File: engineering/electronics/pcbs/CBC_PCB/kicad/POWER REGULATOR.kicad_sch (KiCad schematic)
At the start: 69 parts, among them U23 MP9486GN-Z, U27 10mΩ, U29 1uF, U30 1uH, U9 120pF

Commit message: fix: restore CBC schematic library nicknames
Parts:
- C15: symbol CBC_PCB:CC0805KRX7R0BB471 -> EasyEDA_Lib:CC0805KRX7R0BB471
- C35, C41, C43, C44, C45: symbol CBC_PCB:CL10B104KC8NNNC -> EasyEDA_Lib:CL10B104KC8NNNC
- C37, C39, C62, C75, C76: symbol CBC_PCB:ERJ1KM2R2D11OT -> EasyEDA_Lib:ERJ1KM2R2D11OT
- C38, C40, C74: symbol CBC_PCB:CL21A475KBQNNNE -> EasyEDA_Lib:CL21A475KBQNNNE
- C42, C46: symbol CBC_PCB:TAJB106K025RNJ -> EasyEDA_Lib:TAJB106K025RNJ
- C59, C60, C61, C7, C73: symbol CBC_PCB:GRM31CC72A475KE11L -> EasyEDA_Lib:GRM31CC72A475KE11L
- C63: symbol CBC_PCB:CL10B224KB8NNNC -> EasyEDA_Lib:CL10B224KB8NNNC
- C64, C66, C69, C70, C71, C72, C77: symbol CBC_PCB:GRM31CR61E476ME44L -> EasyEDA_Lib:GRM31CR61E476ME44L
- C65: symbol CBC_PCB:CL10B333KB8NNNC -> EasyEDA_Lib:CL10B333KB8NNNC
- C67: symbol CBC_PCB:CL10C470JB8NNNC -> EasyEDA_Lib:CL10C470JB8NNNC
- C68: symbol CBC_PCB:AC0603KRX7R0BB472 -> EasyEDA_Lib:AC0603KRX7R0BB472
- D14: symbol CBC_PCB:FSV10150V -> EasyEDA_Lib:FSV10150V
- D15: symbol CBC_PCB:SMBJ5.0CA_C83323 -> EasyEDA_Lib:SMBJ5.0CA_C83323
- D16, D19: symbol CBC_PCB:BAV20W-7-F -> EasyEDA_Lib:BAV20W-7-F
- D17: symbol CBC_PCB:SMBJ85A-13-F -> EasyEDA_Lib:SMBJ85A-13-F
- D18: symbol CBC_PCB:CMMR1U-02 TR PBFREE -> EasyEDA_Lib:CMMR1U-02 TR PBFREE
- D20: symbol CBC_PCB:SMB5350B -> EasyEDA_Lib:SMB5350B
- D21: symbol CBC_PCB:SMBJ5365B-TP -> EasyEDA_Lib:SMBJ5365B-TP
- L4: symbol CBC_PCB:ZEMS0850-330M -> EasyEDA_Lib:ZEMS0850-330M
- L5: symbol CBC_PCB:PA1736NL -> EasyEDA_Lib:PA1736NL
- L6: symbol CBC_PCB:PSPMAA1082T-220M-CGP -> EasyEDA_Lib:PSPMAA1082T-220M-CGP
- Q8, Q9: symbol CBC_PCB:SP015N03BGHTO -> EasyEDA_Lib:SP015N03BGHTO
- R30, R33: symbol CBC_PCB:RT0603BRD0710KL -> EasyEDA_Lib:RT0603BRD0710KL
- R31: symbol CBC_PCB:RT0603BRE07240KL -> EasyEDA_Lib:RT0603BRE07240KL
- R32: symbol CBC_PCB:PTFR0603B140KP9 -> EasyEDA_Lib:PTFR0603B140KP9
- R36: symbol CBC_PCB:RC0402FR-070RL -> EasyEDA_Lib:RC0402FR-070RL
- R37: symbol CBC_PCB:FRC0805F1204TS -> EasyEDA_Lib:FRC0805F1204TS
- R38: symbol CBC_PCB:PTFR0603B51K0P9 -> EasyEDA_Lib:PTFR0603B51K0P9
- R39: symbol CBC_PCB:0805W8F1603T5E -> EasyEDA_Lib:0805W8F1603T5E
- R40: symbol CBC_PCB:0603WAF6041T5E -> EasyEDA_Lib:0603WAF6041T5E
- R41, R45: symbol CBC_PCB:0805W8F300KT5E -> EasyEDA_Lib:0805W8F300KT5E
- R42: symbol CBC_PCB:FRC0603F7501TS -> EasyEDA_Lib:FRC0603F7501TS
- R43: symbol CBC_PCB:0603WAF6042T5E -> EasyEDA_Lib:0603WAF6042T5E
- R44: symbol CBC_PCB:FRC0603F2371TS -> EasyEDA_Lib:FRC0603F2371TS
- R5: symbol CBC_PCB:PTFR0603B100RN9 -> EasyEDA_Lib:PTFR0603B100RN9
- R6: symbol CBC_PCB:ERA6AEB680V -> EasyEDA_Lib:ERA6AEB680V
- U23: symbol CBC_PCB:MP9486GN-Z -> MP9486GN-Z:MP9486GN-Z
- U24: symbol CBC_PCB:AMS1117-3.3 -> EasyEDA_Lib:AMS1117-3.3
- U27: symbol CBC_PCB:YLRY06-1-10F -> EasyEDA_Lib:YLRY06-1-10F
- U28: symbol CBC_PCB:LT8309ES5#TRMPBF -> EasyEDA_Lib:LT8309ES5#TRMPBF
- U29: symbol CBC_PCB:CC0805KKX7R0BB105 -> EasyEDA_Lib:CC0805KKX7R0BB105
- U30: symbol CBC_PCB:XAL6030-102MEC -> EasyEDA_Lib:XAL6030-102MEC
- U8: symbol CBC_PCB:LT3748EMS#PBF -> EasyEDA_Lib:LT3748EMS#PBF
- U9: symbol CBC_PCB:GCM1885C2A121FA16D -> EasyEDA_Lib:GCM1885C2A121FA16D
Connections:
- net +3V3: now also C45.1, C46.1, U24.2 (VOUT), U24.4 (VOUT)
- net +5V: now also C35.2, C38.2, C40.2, C42.1, C44.1, C74.2, L4.2, R31.2, U24.3 (VIN)
- net 12V_ISOLATED: now also C71.2, C72.2, C75.1, C76.1, C77.2, D20.1, U30.2
- net GND: now also C15.1, C37.2, C38.1, C39.2, C40.1, C42.2, C43.1, C44.2, C45.2, C46.2, C59.1, C60.1, C61.1, C62.2, C63.1, C64.1, C65.1, C67.1, C68.1, C7.1, C74.1, D14.1 (A), D14.2 (A), D15.1 (K), L5.6, R30.1, R33.1, R38.1, R40.1, R43.1, U23.8 (GND), U24.1 (GND), U27.1, U8.8 (GND), U8.9 (GND)
- net GNDE: now also C66.1, C68.2, C69.1, C70.1, C71.1, C72.1, C73.1, C75.2, C76.2, C77.1, D20.2, D21.2 (A), Q9.2 (S), Q9.3 (S), Q9.4 (S), Q9.5 (S), Q9.6 (S), Q9.7 (S), Q9.8 (S), U28.2 (GND), U29.1
- net H_PWR-IN: now also C37.1, C39.1, C64.2, L6.1, R32.2, U23.3 (VIN)
- net INTVCC: now also C61.2, R6.1, U8.5 (INTVCC)
- new net: C73.2, U28.3 (INTVCC)
- new net: C59.2, C60.2, C62.1, C7.2, D17.2 (A), L5.3, L5.4, L6.2, R37.2, R5.2, U8.1 (VIN)
- new net: Q8.1 (G), R36.2
- new net: Q8.2 (S), Q8.3 (S), Q8.4 (S), Q8.5 (S), Q8.6 (S), Q8.7 (S), Q8.8 (S), R41.2, U27.2
- new net: D18.2 (A), L5.1, L5.2, Q8.9 (D), R39.2, U9.1
- new net: C41.1, D14.3 (K), L4.1, U23.5 (SW)
- new net: R43.2, U8.12 (TC)
- new net: C15.2, R42.2, U8.11 (VC)
- new net: C66.2, C69.2, C70.2, L5.10, L5.11, L5.12, U30.1
- new net: R5.1, U9.2
- new net: C35.1, R30.2, R31.1, U23.1 (FB)
- new net: D17.1 (K), D18.1 (K)
- new net: D19.2 (A), L5.7, L5.8, L5.9, Q9.9 (D), R44.1
- new net: R44.2, U28.5 (DRAIN)
- new net: C67.2, R41.1, U8.7 (SENSE)
- new net: C65.2, R42.1
- new net: D16.1 (C), R6.2
- new net: Q9.1 (G), U28.1 (GATE)
- new net: D21.1 (K), R45.2, U28.4 (VCC), U29.2
- new net: C63.2, U8.10 (SS)
- new net: C43.2, D15.2 (A), R32.1, R33.2, U23.6 (DIM), U23.7 (EN)
- new net: R39.1, U8.16 (RFB)
- new net: D16.2 (A), L5.5
- new net: R40.2, U8.14 (RREF)
- new net: R37.1, R38.2, U8.3 (EN/UVLO)
- new net: C41.2, U23.4 (BST)
- new net: R36.1, U8.6 (GATE)
- new net: D19.1 (C), R45.1

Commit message: fix: qualify CBC connector footprint refs
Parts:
- U23: footprint SOIC-8EP_MP9486_MNP -> CBC_PCB:SOIC-8EP_MP9486_MNP

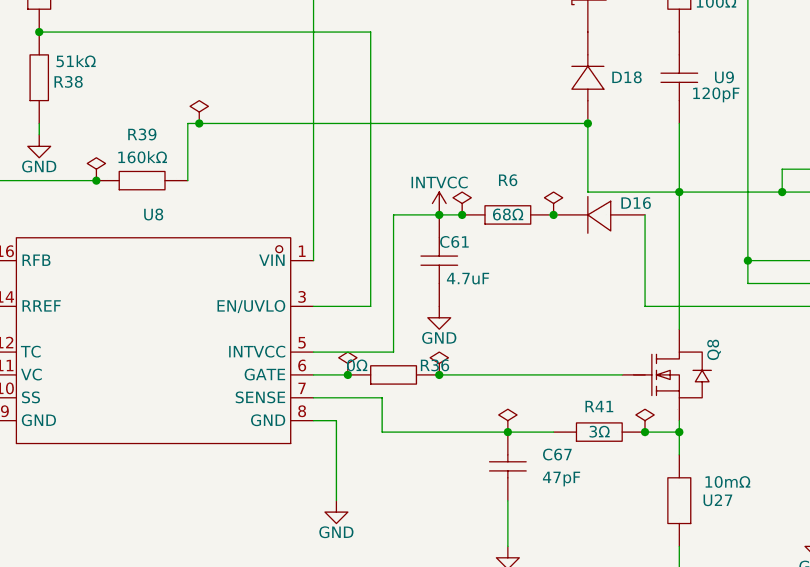
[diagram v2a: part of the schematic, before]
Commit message: fix: assign CBC imported symbol pin types
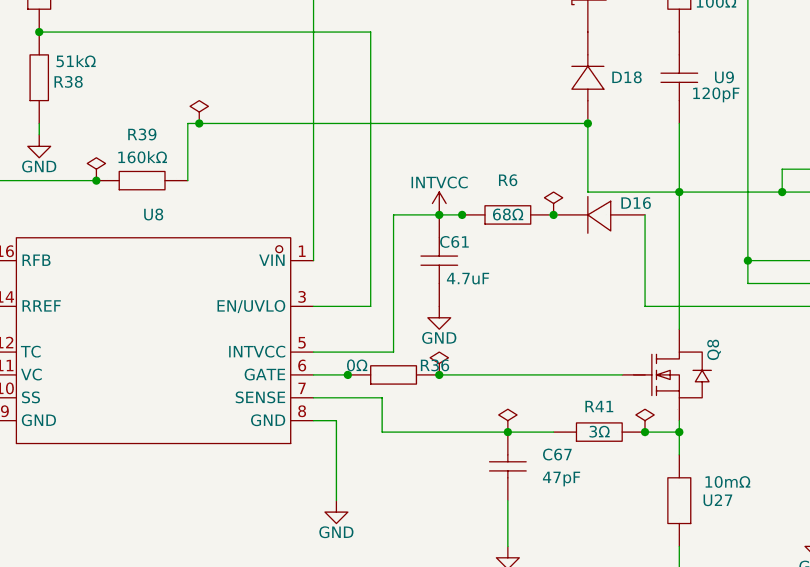
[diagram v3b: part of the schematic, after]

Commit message: electronics: update CBC redundant power regulators
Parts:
- added C100, C101, C103, C95, C96: 100nF, EasyEDA_Lib:C0603, symbol EasyEDA_Lib:CL10B104KC8NNNC
- added C102, C104: 10uF, EasyEDA_Lib:CAP-SMD_L3.5-W2.8-R-RD, symbol EasyEDA_Lib:TAJB106K025RNJ
- added C93, C94: 2.2uF, EasyEDA_Lib:CAP-TH_BD5.0-P2.00-D0.5-FD-1, symbol EasyEDA_Lib:ERJ1KM2R2D11OT
- added C97, C98, C99: 4.7uF, EasyEDA_Lib:C0805, symbol EasyEDA_Lib:CL21A475KBQNNNE
- added D28: (no value), EasyEDA_Lib:TO-277A_L5.9-W4.4-LS6.5-TR, symbol EasyEDA_Lib:FSV10150V
- added D29: (no value), EasyEDA_Lib:SMB_L4.6-W3.6-LS5.3-BI, symbol EasyEDA_Lib:SMBJ5.0CA_C83323
- added L9: 33uH, EasyEDA_Lib:IND-SMD_L8.5-W8.0_SMS0850, symbol EasyEDA_Lib:ZEMS0850-330M
- added R17, R18, R19, R62: 100Ω, EasyEDA_Lib:R0603, symbol EasyEDA_Lib:PTFR0603B100RN9
- added R58: 240kΩ, EasyEDA_Lib:R0603, symbol EasyEDA_Lib:RT0603BRE07240KL
- added R59, R61: 10kΩ, EasyEDA_Lib:R0603, symbol EasyEDA_Lib:RT0603BRD0710KL
- added R60: 140kΩ, EasyEDA_Lib:R0603, symbol EasyEDA_Lib:PTFR0603B140KP9
- added U15, U37, U38, U39: MAX40203AUK+T, EasyEDA_Lib:MAX40203AUK_T_SOT-23-5, symbol EasyEDA_Lib:MAX40203AUK+T
- added U35: MP9486GN-Z, CBC_PCB:SOIC-8EP_MP9486_MNP, symbol MP9486GN-Z:MP9486GN-Z
- added U36: (no value), EasyEDA_Lib:SOT-223-3_L6.5-W3.4-P2.30-LS7.0-BR, symbol EasyEDA_Lib:AMS1117-3.3
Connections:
- net +3V3: now also C101.1, C102.1, U36.2 (VOUT), U38.5 (OUT), U39.5 (OUT); no longer U24.4 (VOUT)
- net +5V: now also C103.1, C104.1, U15.5 (OUT), U36.3 (VIN), U37.5 (OUT); no longer C35.2, C38.2, C40.2, C74.2, L4.2, R31.2
- net GND: now also C100.1, C101.2, C102.2, C103.2, C104.2, C93.2, C94.2, C97.1, C98.1, C99.1, D28.1 (A), D28.2 (A), D29.1 (K), R59.1, R61.1, U15.2 (GND), U35.8 (GND), U36.1 (GND), U37.2 (GND), U38.2 (GND), U39.2 (GND)
- net H_PWR-IN: now also C93.1, C94.1, R60.2, U35.3 (VIN)
- new net: C96.1, R58.1, R59.2, U35.1 (FB)
- new net: R62.2, U39.3 (EN)
- new net: R19.2, U38.3 (EN)
- new net: R18.2, U37.3 (EN)
- new net: C100.2, D29.2 (A), R60.1, R61.2, U35.6 (DIM), U35.7 (EN)
- new net: C95.1, D28.3 (K), L9.1, U35.5 (SW)
- new net: R17.2, U15.3 (EN)
- new net: C95.2, U35.4 (BST)
- new net +3V3_P1: R19.1, U24.4 (VOUT), U38.1 (VDD)
- new net +3V3_P2: U36.4 (VOUT)
- new net +5V_P1: C35.2, C38.2, C40.2, C74.2, L4.2, R17.1, R31.2, U15.1 (VDD)
- new net +5V_P2: C96.2, C97.2, C98.2, C99.2, L9.2, R18.1, R58.2, R62.1, U37.1 (VDD), U39.1 (VDD)
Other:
- moved on the sheet: C15, C42, C44, C45, C46, C59, C60, C61, C62, C63, C64, C65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
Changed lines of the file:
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@@
 	(generator "eeschema")
 	(generator_version "10.0")
-	(paper "A4")
+	(paper "A3")
